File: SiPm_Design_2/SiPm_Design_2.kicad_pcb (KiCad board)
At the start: 2 copper layers, 27 parts, among them IC1 OPA354AIDDAR, IC2 OPA354AIDDAR, IC3 OPA354AIDDAR, IC4 AFBR-S4N44P014M

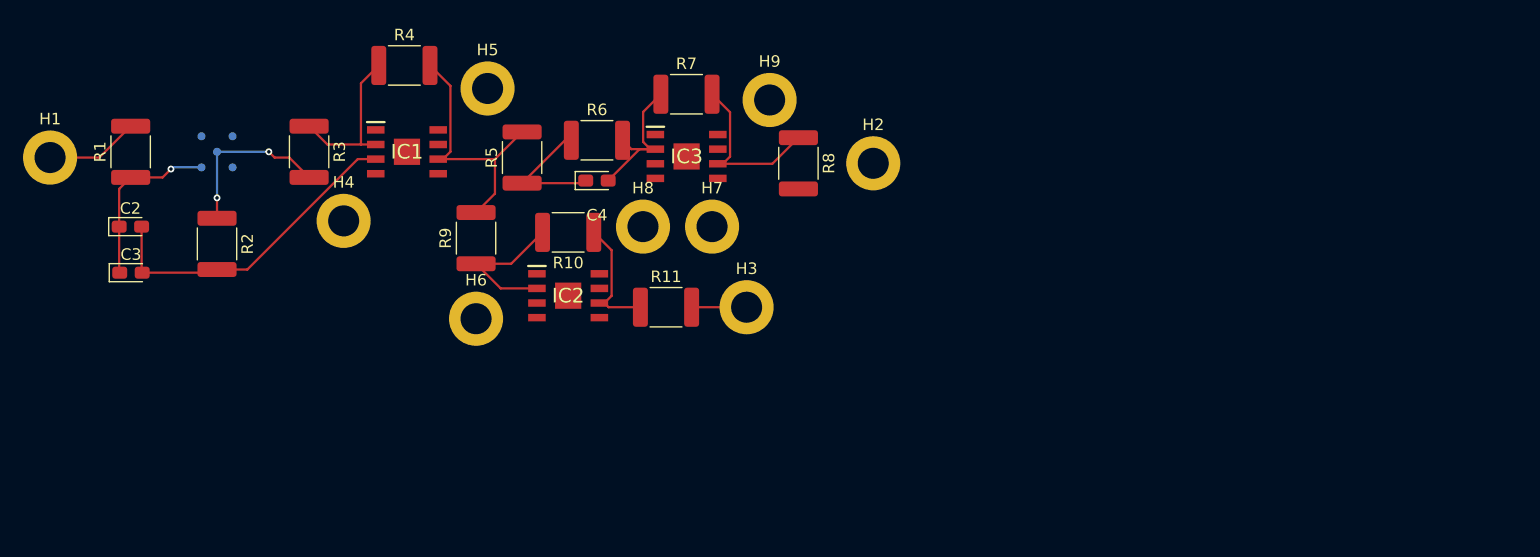
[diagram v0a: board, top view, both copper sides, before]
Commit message: change footprint of some res cap
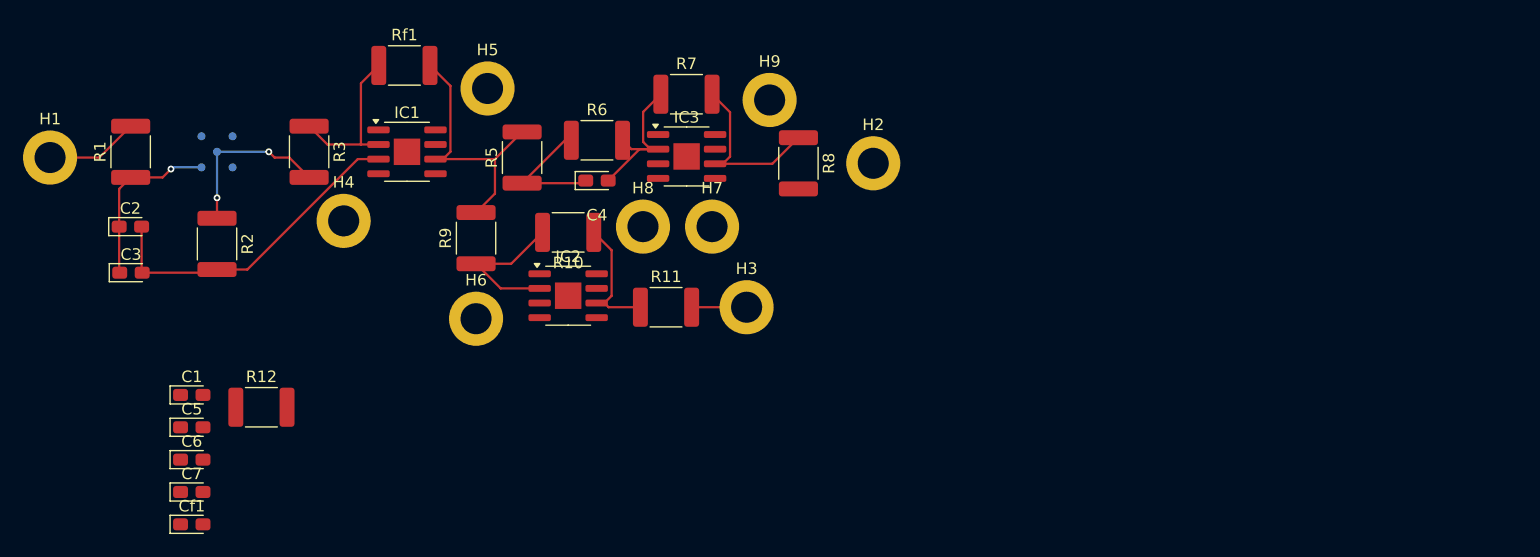
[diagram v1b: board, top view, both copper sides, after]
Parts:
- added C1: 100n, Capacitor_Tantalum_SMD:CP_EIA-2012-12_Kemet-R_Pad1.30x1.05mm_HandSolder, F.Cu at (139.8, 106.1)
- added C5: 100n, Capacitor_Tantalum_SMD:CP_EIA-2012-12_Kemet-R_Pad1.30x1.05mm_HandSolder, F.Cu at (139.8, 108.9)
- added C6: 100n, Capacitor_Tantalum_SMD:CP_EIA-2012-12_Kemet-R_Pad1.30x1.05mm_HandSolder, F.Cu at (139.8, 111.7)
- added C7: 100n, Capacitor_Tantalum_SMD:CP_EIA-2012-12_Kemet-R_Pad1.30x1.05mm_HandSolder, F.Cu at (139.8, 114.5)
- added Cf1: 1n, Capacitor_Tantalum_SMD:CP_EIA-2012-12_Kemet-R_Pad1.30x1.05mm_HandSolder, F.Cu at (139.8, 117.4)
- added R12: 47, Resistor_SMD:R_1812_4532Metric_Pad1.30x3.40mm_HandSolder, F.Cu at (145.9, 107.2)
- IC1, IC2, IC3: footprint OPA354:SOIC127P600X170-9N -> Package_SO:HSOP-8-1EP_3.9x4.9mm_P1.27mm_EP2.3x2.3mm
- IC4: footprint KiCad:AFBRS4N44P014M -> S4N44P014M:AFBRS4N44P014M
- renumbered R4 to Rf1
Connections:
- IC1 pad 3: Earth -> Net-(IC1-+IN)
- IC1 pad 4: Net-(IC1-V-) -> -2V5
- IC1 pad 7: Net-(IC1-V+) -> +2V5
- IC2 pad 4: Net-(IC2-V-) -> -2V5
- IC2 pad 7: Net-(IC2-V+) -> +2V5
- IC3 pad 4: unconnected-(H8-Pad1) -> -2V5
- IC3 pad 7: unconnected-(H9-Pad1) -> +2V5

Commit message: change to 2 opamp
add connector
change to OPA2354
done layout as 2 layers
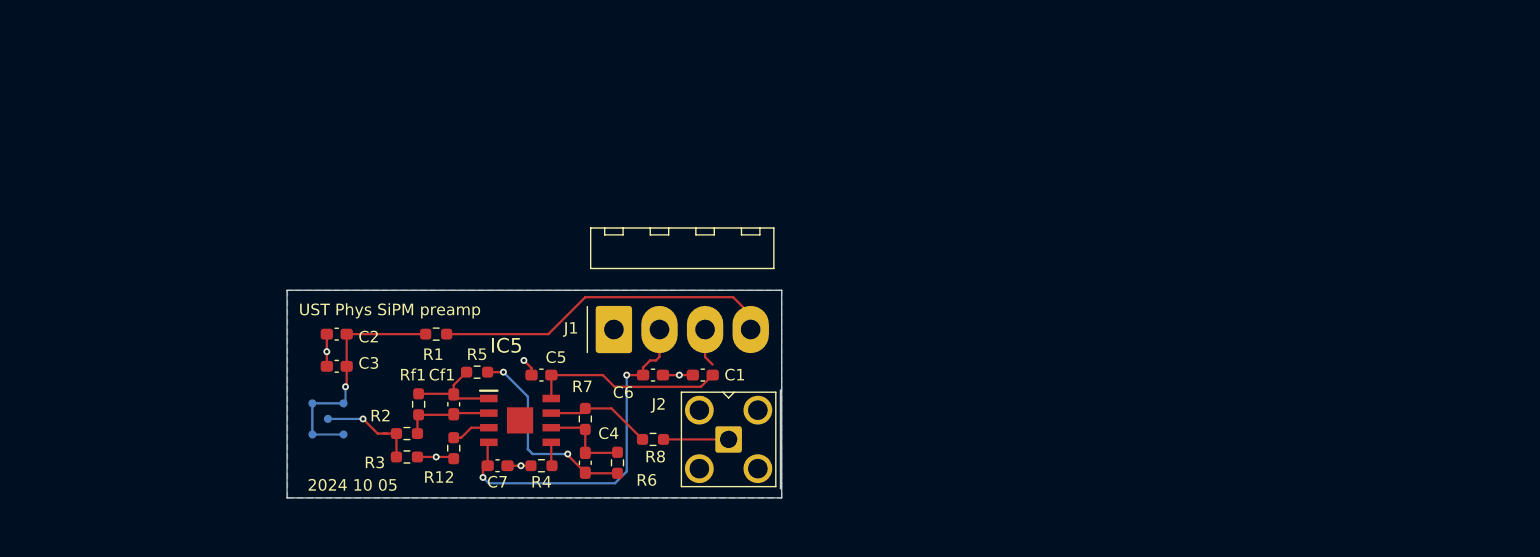
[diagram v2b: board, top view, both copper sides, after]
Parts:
- removed H1, H2, H3, H4, H5, H6, H7, H8, H9: MountingHole_Pad, MountingHole:MountingHole_2.7mm_M2.5_DIN965_Pad
- removed IC1, IC2, IC3: OPA354AIDDAR, Package_SO:HSOP-8-1EP_3.9x4.9mm_P1.27mm_EP2.3x2.3mm
- removed R10: 440, Resistor_SMD:R_1812_4532Metric_Pad1.30x3.40mm_HandSolder
- removed R11: 47, Resistor_SMD:R_1812_4532Metric_Pad1.30x3.40mm_HandSolder
- removed R9: 20, Resistor_SMD:R_1812_4532Metric_Pad1.30x3.40mm_HandSolder
- added IC5: OPA2354AIDDARG3, LIB_OPA2354AIDDARG3:SOIC127P600X170-9N, F.Cu at (168.3, 108.3)
- added J1: Conn_01x04_Pin, Connector_Molex:Molex_KK-396_A-41792-0004_1x04_P3.96mm_Horizontal, F.Cu at (176.5, 100.4)
- added J2: Conn_Coaxial_Small, Connector_Coaxial:SMA_Amphenol_901-143_Horizontal, F.Cu at (186.4, 110.0)
- added R4: 47, Resistor_SMD:R_0603_1608Metric_Pad0.98x0.95mm_HandSolder, F.Cu at (170.2, 112.3)
- C1, C2, C3, C4, C6, Cf1: footprint Capacitor_Tantalum_SMD:CP_EIA-2012-12_Kemet-R_Pad1.30x1.05mm_HandSolder -> Capacitor_SMD:C_0603_1608Metric_Pad1.08x0.95mm_HandSolder
- C5, C7: value 100n -> 10n; footprint Capacitor_Tantalum_SMD:CP_EIA-2012-12_Kemet-R_Pad1.30x1.05mm_HandSolder -> Capacitor_SMD:C_0603_1608Metric_Pad1.08x0.95mm_HandSolder
- R1, R12, R2, R3, R5, R6, R7, R8, Rf1: footprint Resistor_SMD:R_1812_4532Metric_Pad1.30x3.40mm_HandSolder -> Resistor_SMD:R_0603_1608Metric_Pad0.98x0.95mm_HandSolder
- moved C1 44.4 mm to (184.2, 104.4), turned to 180 degrees
- moved C6 40.7 mm to (179.9, 104.4), turned to 180 degrees
- moved R1 30.9 mm to (161.0, 100.8), turned to 0 degrees
- moved C5 30.7 mm to (170.2, 104.4), turned to 180 degrees
- moved R7 29.5 mm to (174.0, 108.2), turned to 90 degrees
- moved Rf1 29.5 mm to (159.5, 106.9), turned to 90 degrees
- moved R6 28.1 mm to (176.8, 112.0), turned to 90 degrees
- moved R8 27.1 mm to (179.9, 110.0), turned to 0 degrees
- moved C7 26.7 mm to (166.4, 112.3), turned to 180 degrees
- moved R3 25.9 mm to (158.5, 109.5), turned to 180 degrees
- moved IC4 25.1 mm to (151.6, 108.2)
- moved Cf1 25.0 mm to (162.6, 106.9), turned to 90 degrees
- moved R2 24.8 mm to (158.5, 111.5), turned to 0 degrees
- moved C4 24.5 mm to (174.0, 112.0), turned to 90 degrees
- moved C2 20.2 mm to (152.4, 100.8), turned to 180 degrees
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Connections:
- IC4 pad A3: unconnected-(IC4-CATHODE_2-PadA3) -> Net-(IC4-CATHODE_1)
- IC4 pad C1: unconnected-(IC4-CATHODE_3-PadC1) -> Net-(IC4-CATHODE_1)
- IC4 pad C3: unconnected-(IC4-CATHODE_4-PadC3) -> Net-(IC4-CATHODE_1)
- R8 pad 2: Earth -> Net-(J2-In)
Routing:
- net Earth: track 43.9 -> 12.2 mm, vias 0 -> 5
- net -2V5: track 0.00 -> 31.0 mm, vias 0 -> 2
- net V_bias: track 8.13 -> 29.8 mm
- net +2V5: track 0.00 -> 20.2 mm
- net Net-(IC5-OUT_A): track 23.1 -> 8.66 mm
- net Net-(IC2--IN): track 13.1 -> 0.00 mm
- net Net-(IC5--IN_B): track 14.5 -> 7.87 mm
- net Net-(C4-Pad1): track 11.4 -> 17.7 mm, vias 0 -> 2
- net Net-(IC5--IN_A): track 14.0 -> 7.83 mm
- net Net-(IC5-OUT_B): track 15.3 -> 9.21 mm
- net Net-(IC4-ANODE): track 14.7 -> 8.76 mm, vias 2 -> 1
- net Net-(IC4-CATHODE_1): track 15.2 -> 21.1 mm
- net Net-(J2-In): track 0.00 -> 5.65 mm
- net Net-(IC5-+IN_A): track 0.00 -> 3.41 mm
- net Net-(IC5-+IN_B): track 0.00 -> 2.06 mm
- added copper zone on B.Cu, net Earth
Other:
- board outline added: 43 x 18 mm
- board text added: "2024 10 05"
- board text added: "UST Phys SiPM preamp"

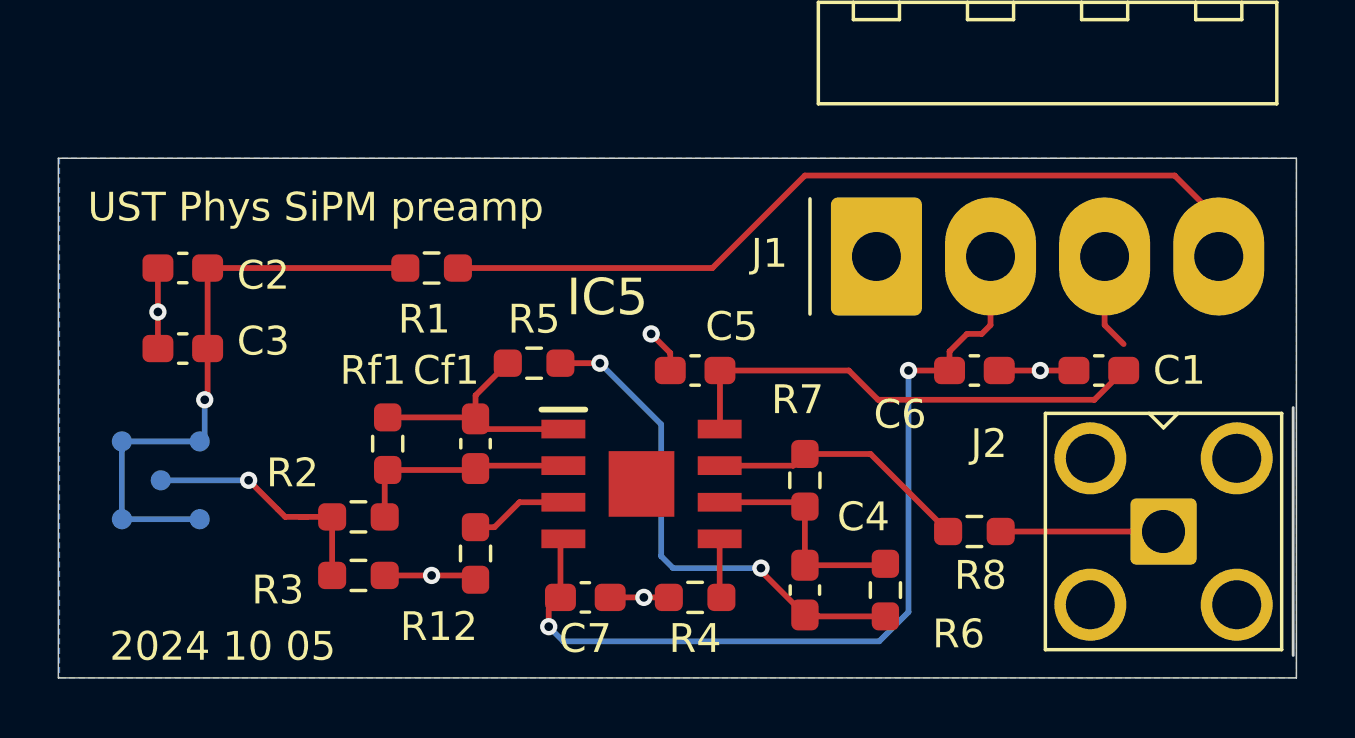
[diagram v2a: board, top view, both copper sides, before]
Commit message: add top fill, smaller font, SiPM hole
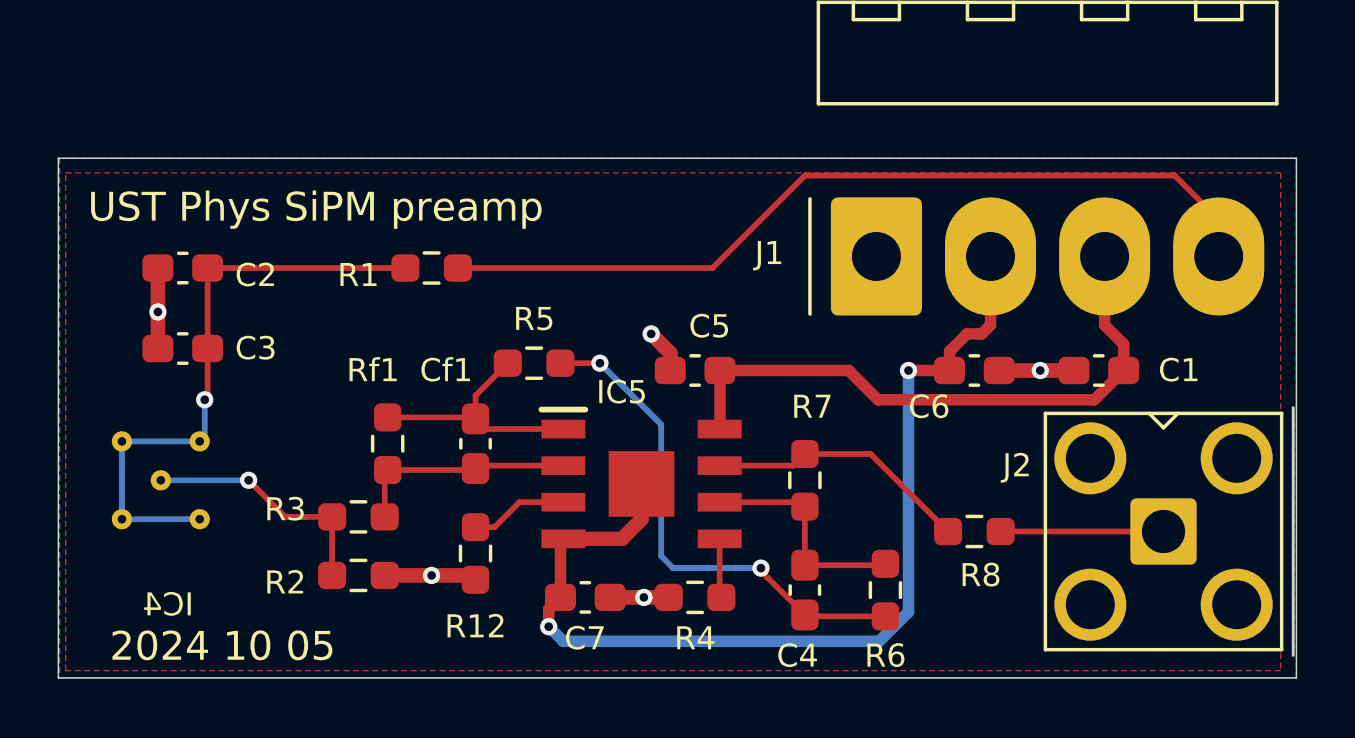
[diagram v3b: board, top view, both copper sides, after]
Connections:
- IC5 pad 9: unconnected-(IC5-EP-Pad9) -> -2V5
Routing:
- net -2V5: track 31.0 -> 35.2 mm
- net +2V5: track 20.2 -> 21.1 mm
- added copper zone on F.Cu, net Earth

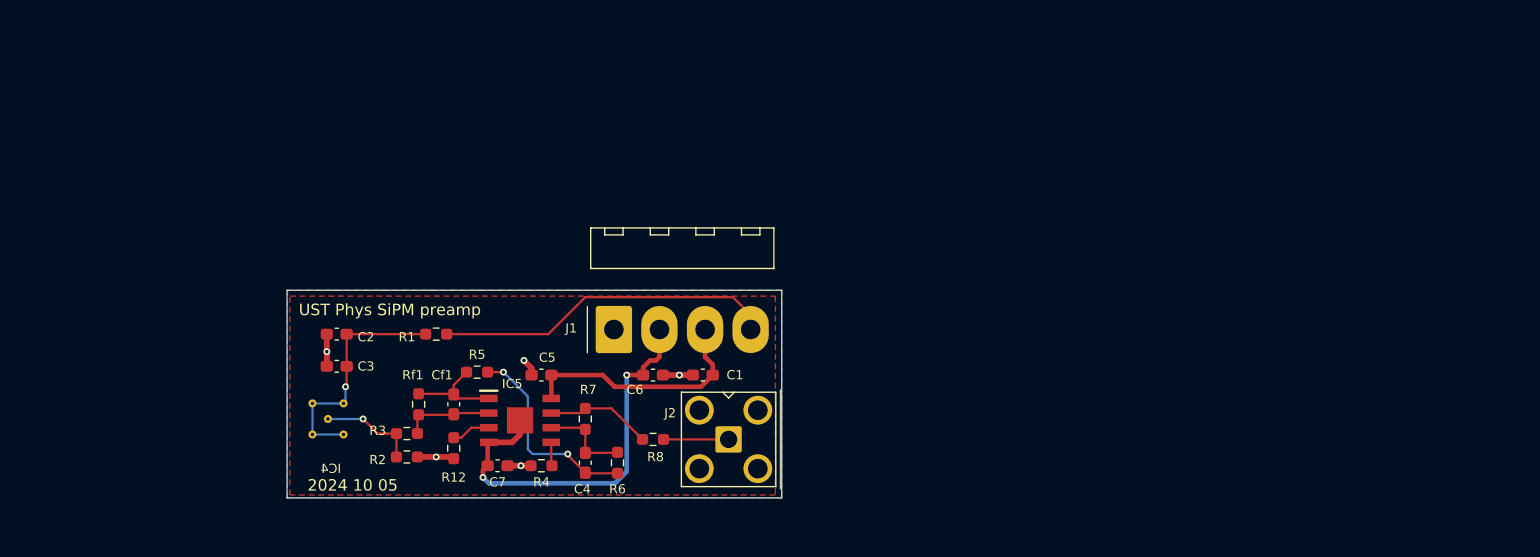
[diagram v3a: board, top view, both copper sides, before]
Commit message: 1 Amp, flex , redesign
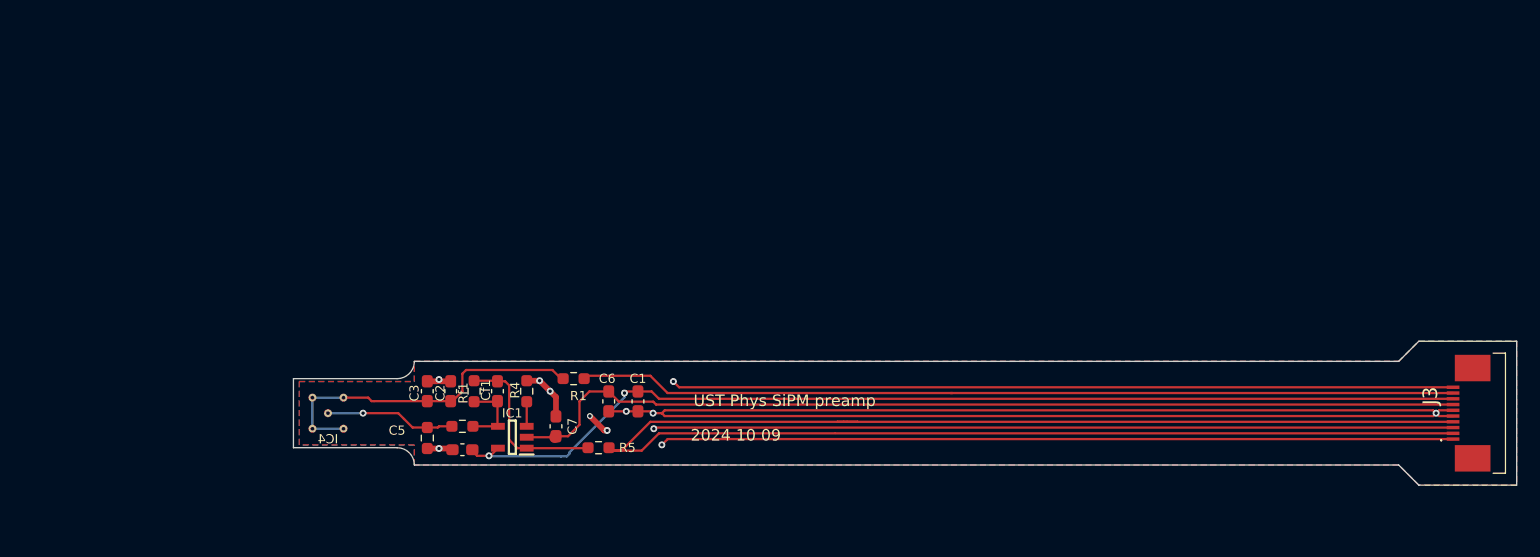
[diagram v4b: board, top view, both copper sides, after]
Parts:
- removed C4: 10p, Capacitor_SMD:C_0603_1608Metric_Pad1.08x0.95mm_HandSolder
- removed IC5: OPA2354AIDDARG3, LIB_OPA2354AIDDARG3:SOIC127P600X170-9N
- removed J1: Conn_01x04_Pin, Connector_Molex:Molex_KK-396_A-41792-0004_1x04_P3.96mm_Horizontal
- removed J2: Conn_Coaxial_Small, Connector_Coaxial:SMA_Amphenol_901-143_Horizontal
- removed R12, R8: 47, Resistor_SMD:R_0603_1608Metric_Pad0.98x0.95mm_HandSolder
- removed R6: 5.1k, Resistor_SMD:R_0603_1608Metric_Pad0.98x0.95mm_HandSolder
- removed R7: 1k, Resistor_SMD:R_0603_1608Metric_Pad0.98x0.95mm_HandSolder
- added IC1: OPA354AIDBVTG4, LIB_OPA354AIDBVTG4:SOT95P280X145-5N, F.Cu at (167.7, 109.8)
- added J3: 1-1734839-0, FPC 0.5 10P:117348390, F.Cu at (251.6, 107.7)
- Cf1: value 1n -> 10p
- R2, R4, R5: value 47 -> 50
- R3: value 10 -> 0
- moved R1 12.5 mm to (173.0, 104.7)
- moved R5 12.4 mm to (175.1, 110.7)
- moved C2 11.1 mm to (162.3, 105.8), turned to 90 degrees
- moved C5 9.44 mm to (163.3, 110.9)
- moved C3 8.16 mm to (160.3, 105.8), turned to 90 degrees
- moved R4 6.60 mm to (168.9, 105.8), turned to 90 degrees
- moved C7 6.12 mm to (171.4, 108.8), turned to -90 degrees
- moved C1 6.07 mm to (178.6, 106.7), turned to -90 degrees
- moved Rf1 4.95 mm to (164.3, 105.8)
- moved R3 4.86 mm to (163.3, 108.8)
- moved C6 4.48 mm to (176.0, 106.7), turned to 90 degrees
- moved Cf1 3.97 mm to (166.4, 105.8)
- moved R2 2.42 mm to (160.3, 109.9), turned to -90 degrees
- moved IC4 0.50 mm to (151.6, 107.7)
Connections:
- net Net-(IC5--IN_A) renamed /IN_n
- net Net-(IC5-OUT_A) renamed /Vout
- R4 pad 1: Net-(IC5-+IN_B) -> /IN_p
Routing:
- net Earth: track 12.2 -> 360.3 mm, vias 5 -> 12
- net Net-(J3-Pad2): track 17.7 -> 149.8 mm, vias 2 -> 0
- net +2V5: track 21.1 -> 89.6 mm, vias 0 -> 2
- net -2V5: track 35.2 -> 83.8 mm, vias 2 -> 0
- net V_bias: track 29.8 -> 75.9 mm
- net Net-(IC5-OUT_B): track 9.21 -> 0.00 mm
- net Net-(IC4-CATHODE_1): track 21.1 -> 29.2 mm, vias 1 -> 0
- net Net-(IC5--IN_B): track 7.87 -> 0.00 mm
- net /Vout: track 8.66 -> 15.1 mm
- net Net-(J2-In): track 5.65 -> 0.00 mm
- net Net-(IC5-+IN_A): track 3.41 -> 0.00 mm
- net Net-(IC4-ANODE): track 8.76 -> 11.3 mm
- net /IN_p: track 0.00 -> 2.14 mm
- net Net-(IC5-+IN_B): track 2.06 -> 0.00 mm
- net /IN_n: track 7.83 -> 6.43 mm
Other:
- board size 43 x 18 mm -> 106.2 x 12.5 mm
- board text added: "2024 10 09"
- board text removed: "2024 10 05"

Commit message: ran through design rule
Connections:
- J3 pad MP1: unconnected-(J3-PadMP1) -> Earth
- J3 pad MP2: unconnected-(J3-PadMP2) -> Earth
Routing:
- net Earth: vias 12 -> 16
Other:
- copper layers 2 -> 4

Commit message: gerber to JLC
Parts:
- added R6: 50, Resistor_SMD:R_0603_1608Metric_Pad0.98x0.95mm_HandSolder, F.Cu at (178.6, 110.7)
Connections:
- R5 pad 1: Net-(J3-Pad2) -> Net-(R5-Pad1)
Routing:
- net Net-(R5-Pad1): track 0.00 -> 4.05 mm, vias 0 -> 1
- net Net-(J3-Pad2): track 150.0 -> 148.7 mm, vias 0 -> 1
- net Earth: track 360.3 -> 360.1 mm, vias 16 -> 17
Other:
- copper layers 4 -> 2
- board text added: "2024 10 14"
- board text added: "EM shielding film"
- board text added: "PI stiffener 0.225mm"
- board text removed: "2024 10 09"

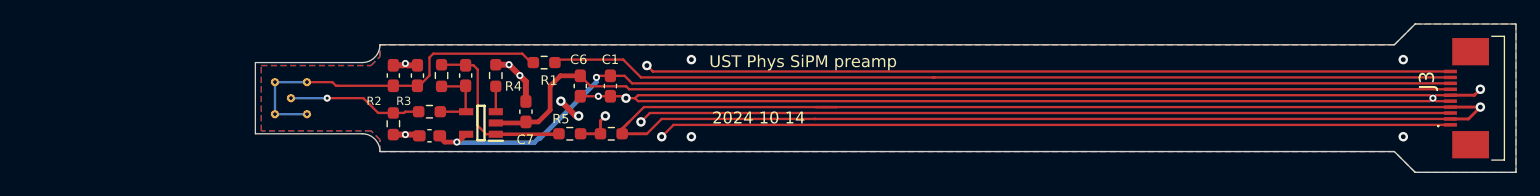
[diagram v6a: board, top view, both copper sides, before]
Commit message: extended SiPM section, 4 mirrored footprints.
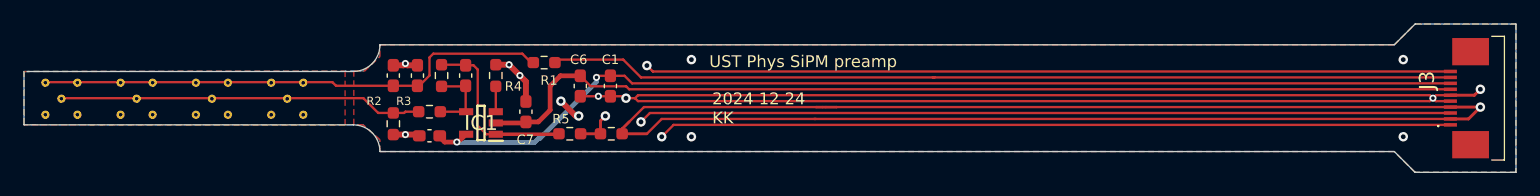
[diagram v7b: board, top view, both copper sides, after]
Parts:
- added IC2: AFBR-S4N44P014M, S4N44P014M:AFBRS4N44P014M, B.Cu at (151.3, 107.8)
- added IC3: AFBR-S4N44P014M, S4N44P014M:AFBRS4N44P014M, B.Cu at (145.0, 107.8)
- added IC5: AFBR-S4N44P014M, S4N44P014M:AFBRS4N44P014M, B.Cu at (132.3, 107.8)
- moved IC4 13.0 mm to (138.6, 107.8)
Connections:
- net Net-(IC4-ANODE) renamed /anode
- net Net-(IC4-CATHODE_1) renamed /Bias
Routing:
- net /anode: track 11.3 -> 30.7 mm, vias 1 -> 0
- net /Bias: track 29.2 -> 43.1 mm
- added copper zone on F.Cu, net /Bias
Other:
- board size 106.2 x 12.5 mm -> 125.8 x 12.5 mm
- board text added: "2024 12 24 KK"
- board text removed: "2024 10 14"
